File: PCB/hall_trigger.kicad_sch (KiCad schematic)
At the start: 2 parts

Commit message: task: write matched LCSC part numbers into the schematic
Adds scripts/apply_lcsc_fields.py, which clones each symbol's existing
Manufacturer_Part_Number property (same indentation/effects) into a new
'LCSC' field with the matched code -- the field name the Fabrication
Toolkit plugin already installed in this repo recognizes for JLCPCB BOM
matching.

Applied the 31 confirmed matches from jlc_match.py across all sheets
(68 individual references). C_BUCK_OUT1 and R_ISET1 are left without an
LCSC field -- JLC doesn't stock those exact Yageo part numbers, to be
sorted out separately.

Verified: kicad-cli sch export bom round-trips every LCSC value
correctly, and ERC reports 0 violations.

Also switched jlc_match.py's BOM export to unranged references so each
match maps cleanly to individual schematic symbols.

Co-Authored-By: Claude Sonnet 5 <noreply@anthropic.com>
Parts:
- C_HALL1: LCSC (none) -> C131394
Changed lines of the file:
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@@
+			)
+		)
+		(property "LCSC" "C131394"
+			(at 0 0 0)
+			(hide yes)
+			(show_name no)
+			(do_not_autoplace no)
+			(effects
+				(font
+					(size 1.27 1.27)
+				)
 			)
 		)

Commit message: task: alert on Basic-library alternatives during JLC part matching (#33)
* task: alert on Basic-library alternatives during JLC part matching

JLC's "Extended" library carries a per-unique-part setup fee on top of
unit price; "Basic" doesn't. That fee doesn't amortize well on a board
with many distinct low-quantity parts -- confirmed the hard way: our
first real JLCPCB assembly quote came back at $333.84 vs PCBWay's
~$190 for the same order, and all 33 of our matched parts were
Extended.

jlc_match.py now does a secondary search for a same-value/same-package
Basic-library part whenever the real match lands on Extended, and
flags it in the report (new BasicAlt column + a Status alert) rather
than silently leaving it. On the current board this surfaces 11
plausible Basic-library swaps (common resistor/cap values, and the
generic 1N4148W diode and 2N7002 MOSFET, which are industry-standard
parts many brands stock identically).

This is alert-only, same as the rest of this script -- it doesn't
touch the schematic. Spot-checked 4 of the 11 suggestions directly
against JLC's catalog to confirm value/package actually match, not
just a keyword hit.

Co-Authored-By: Claude Sonnet 5 <noreply@anthropic.com>

* fix: two correctness bugs in Basic-library alternative matching

1. find_basic_alternative() trusted the raw keyword-search hit without
   verifying the candidate's actual value -- JLC's fuzzy full-text search
   can return a wrong-value part that just shares digits (e.g. searching
   "100 0402" surfaced a 1kΩ resistor, EIA code "1001", as a false match
   for a 100Ω part). Now parses and compares the actual numeric value
   (with unit) before accepting a candidate; falls back to exact
   model-name matching for non-numeric values (generic diode/transistor
   part families like "1N4148W", "2N7002").

2. The new value parser's regex required the unit to be the first
   character of the string, but JLC resistor descriptions carry a
   Chinese prefix ("厚膜电阻 10kΩ ±1%" = "thi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
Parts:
- C_HALL1: LCSC C131394 -> C1525; MF Yageo -> Samsung Electro-Mechanics; Manufacturer_Part_Number CC0402KRX7R9BB104 -> CL05B104KO5NNNC
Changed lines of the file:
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@@
 			)
 		)
-		(property "MF" "Yageo"
+		(property "MF" "Samsung Electro-Mechanics"
 			(at 0 0 0)
 			(hide yes)
@@
 			)
 		)
-		(property "Manufacturer_Part_Number" "CC0402KRX7R9BB104"
+		(property "Manufacturer_Part_Number" "CL05B104KO5NNNC"
 			(at 0 0 0)
 			(hide yes)
@@
 			)
 		)
-		(property "LCSC" "C131394"
+		(property "LCSC" "C1525"
 			(at 0 0 0)
 			(hide yes)

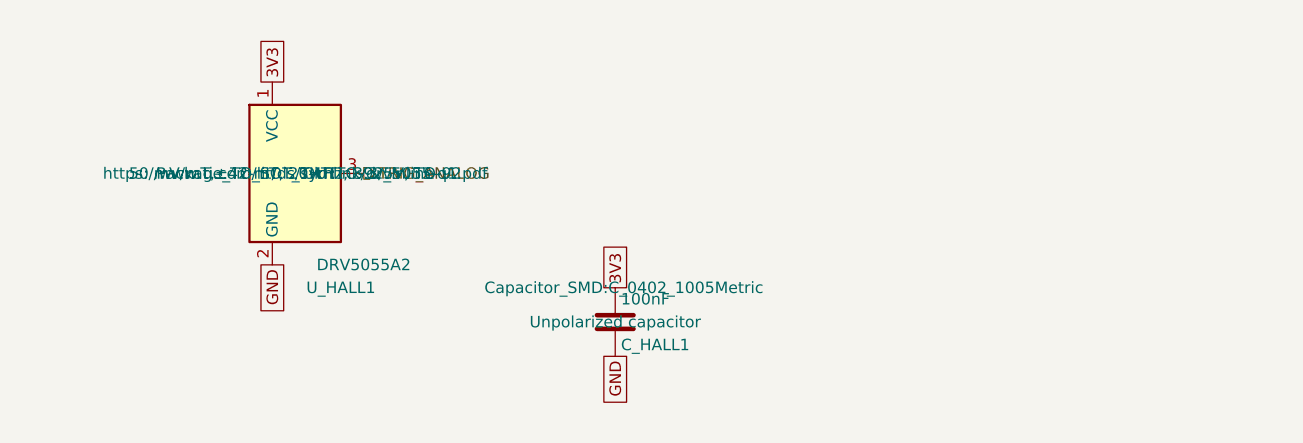
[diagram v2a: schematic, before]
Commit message: fix: make every BOM Value unambiguous for the fab, and switch D_INV_ISO1 to SOT-323 (#61)
* fix: make every BOM Value unambiguous for the fab, and switch D_INV_ISO1 to SOT-323

PCBWay flagged D_INV_ISO1: "BAT54W" is SOT-323 from nearly every maker, but we
had picked Yangjie's SOD-123 variant. A fab only sees Designator, Footprint,
Quantity and Value in the BOM (never MF/MPN/LCSC), so a bare part name is
ambiguous. Fixes the class of problem, not just this part:

- Every component's Value is now "<label> | <MPN> | <manufacturer> | <package>"
  (label dropped when it repeats the MPN; commas/periods stripped so the CSV
  never needs quoting). BT1 keeps its RIGHT-ANGLE HORIZONTAL note. Applied to
  all 81 parts across every sheet and the PCB.
- scripts/bom_values.py builds, applies, and checks these values, including
  that the PCB copy of Value/MF/MPN/footprint matches the schematic. New
  footprints must be added to its package table on purpose; hand-sourced parts
  with no MPN (J_STICK1) are listed explicitly.
- D_INV_ISO1 -> Diodes BAT54W-7-F in SOT-323 (common part, several makers).
  Pin 1 anode / pin 2 not connected / pin 3 cathode, confirmed against
  Nexperia's numbered pinning table and Diodes' datasheet. Uses KiCad's
  Diode:BAT54W symbol; PCB footprint replaced and rerouted. Electrically the
  same BAT54 family (30V, 200mA, 2uA leakage at 25V), so the SPICE model and
  scripts/spice/latch_sim.py still pass.
- Layout diagrams now say AO3401A for Q_PWR1 (they were stale since it was
  swapped from DMG2305UX) and BAT54W-7-F/SOT-323 for D_INV_ISO1.
- Repo CLAUDE.md documents the Value rule and the script.

ERC/DRC clean; production files regenerated.

Co-Authored-By: Claude Sonnet 5 <noreply@anthropic.com>

* chore: commit KiCad project settings (reordered used-designators list)

Co-Authored-By: Claude Sonnet 5 <noreply@anthropic.com>

---------

Co-authored-by: Claude Sonnet 5 <noreply@anthropic.com>
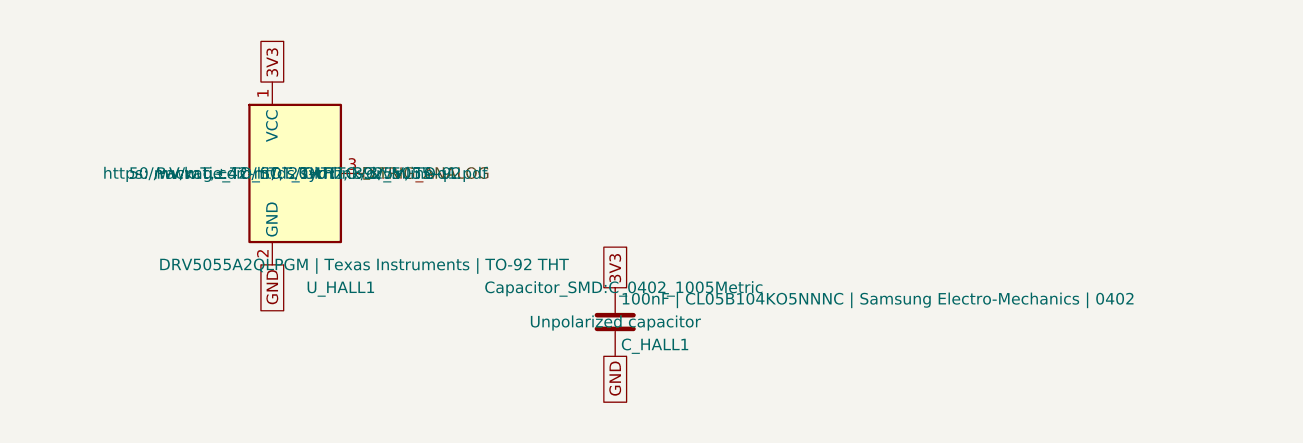
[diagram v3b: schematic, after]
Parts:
- C_HALL1: value 100nF -> 100nF | CL05B104KO5NNNC | Samsung Electro-Mechanics | 0402
- U_HALL1: value DRV5055A2 -> DRV5055A2QLPGM | Texas Instruments | TO-92 THT
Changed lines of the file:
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@@
 			)
 		)
-		(property "Value" "DRV5055A2"
+		(property "Value" "DRV5055A2QLPGM | Texas Instruments | TO-92 THT"
 			(at 138.43 106.68 0)
 			(show_name no)
@@
 			)
 		)
-		(property "Value" "100nF"
+		(property "Value" "100nF | CL05B104KO5NNNC | Samsung Electro-Mechanics | 0402"
 			(at 167.005 110.49 0)
 			(show_name no)
